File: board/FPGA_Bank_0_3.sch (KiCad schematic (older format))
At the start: 13 parts, among them U10 XC6SLX150T

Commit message: Issue #1458 - HDMI RX TX pins added, Cypress added, DDR added
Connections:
- net GTP1V2: now also U10.E9 (MGTRREF_101)
- net TX_LANEN2: now reaches U10.A14 (*MGTTXN0_123)
- net TX_LANEN3: now reaches U10.A16 (*MGTTXN1_123)
- net RXCONFIG1: now reaches U10.A18 (IO_L63N_SCP6_0)
- net TXHPD: now reaches U10.A19 (IO_L64N_SCP4_0)
- net TXAUXCH_N: now reaches U10.A20 (IO_L65N_SCP2_0)
- net TX_LANEN0: now reaches U10.A6 (MGTTXN0_101)
- net TX_LANEN1: now reaches U10.A8 (MGTTXN1_101)
- net TX_LANEP2: now reaches U10.B14 (*MGTTXP0_123)
- net TX_LANEP3: now reaches U10.B16 (*MGTTXP1_123)
- net RXCONFIG2: now reaches U10.B18 (IO_L63P_SCP7_0)
- net TXAUXCH_P: now reaches U10.B20 (IO_L65P_SCP3_0)
- net TX_LANEP0: now reaches U10.B6 (MGTTXP0_101)
- net TX_LANEP1: now reaches U10.B8 (MGTTXP1_101)
- net RX_LANEN2: now reaches U10.C13 (*MGTRXN0_123)
- net RX_LANEN3: now reaches U10.C15 (*MGTRXN1_123)
- net TXCONFIG1: now reaches U10.C18 (IO_L66N_SCP0_0)
- net RXHPD: now reaches U10.C19 (IO_L64P_SCP5_0)
- net RX_LANEN0: now reaches U10.C7 (MGTRXN0_101)
- net RX_LANEN1: now reaches U10.C9 (MGTRXN1_101)
- net RX_LANEP2: now reaches U10.D13 (*MGTRXP0_123)
- net RX_LANEP3: now reaches U10.D15 (*MGTRXP1_123)
- net TXCONFIG2: now reaches U10.D17 (IO_L66P_SCP1_0)
- net RXAUXCH_P: now reaches U10.D18 (IO_L62P_0)
- net RXAUXCH_N: now reaches U10.D19 (IO_L62N_VREF_0)
- net RX_LANEP0: now reaches U10.D7 (MGTRXP0_101)
- net RX_LANEP1: now reaches U10.D9 (MGTRXP1_101)
- net CLK1_N: no longer names the net of U10.B12 (*MGTREFCLK0N_123)
- net CLK1_P: no longer names the net of U10.A12 (*MGTREFCLK0P_123)
- net CLK2_N: no longer names the net of U10.F12 (*MGTREFCLK1N_123)
- net CLK2_P: no longer names the net of U10.E12 (*MGTREFCLK1P_123)
- net GPIO_N_48: no longer names the net of U10.P7 (*IO_L25N_3)
- net GPIO_N_49: no longer names the net of U10.T4 (*IO_L24N_3)
- net GPIO_N_50: no longer names the net of U10.N7 (*IO_L23N_3)
- net GPIO_N_51: no longer names the net of U10.AA1 (IO_L10N_3)
- net GPIO_N_52: no longer names the net of U10.P4 (IO_L9N_3)
- net GPIO_N_53: no longer names the net of U10.V3 (*IO_L8N_3)
- net GPIO_N_54: no longer names the net of U10.T5 (*IO_L7N_3)
- net GPIO_N_55: no longer names the net of U10.Y3 (IO_L2N_3)
- net GPIO_N_56: no longer names the net of U10.G4 (*IO_L58N_3)
- net GPIO_N_57: no longer names the net of U10.D1 (IO_L59N_3)
- net GPIO_N_58: no longer names the net of U10.E4 (IO_L60N_3)
- net GPIO_N_59: no longer names the net of U10.G7 (*IO_L80N_3)
- net GPIO_N_60: no longer names the net of U10.H8 (*IO_L81N_3)
- net GPIO_P_48: no longer names the net of U10.P6 (*IO_L25P_3)
- net GPIO_P_49: no longer names the net of U10.U4 (*IO_L24P_3)
- net GPIO_P_50: no longer names the net of U10.N6 (*IO_L23P_3)
- net GPIO_P_51: no longer names the net of U10.AA2 (IO_L10P_3)
- net GPIO_P_52: no longer names the net of U10.P5 (IO_L9P_3)
- net GPIO_P_53: no longer names the net of U10.V5 (*IO_L8P_3)
- net GPIO_P_54: no longer names the net of U10.T6 (*IO_L7P_3)
- net GPIO_P_55: no longer names the net of U10.W4 (IO_L2P_3)
- net GPIO_P_56: no longer names the net of U10.H4 (*IO_L58P_3)
- net GPIO_P_57: no longer names the net of U10.D2 (IO_L59P_3)
- net GPIO_P_58: no longer names the net of U10.F3 (IO_L60P_3)
- net GPIO_P_59: no longer names the net of U10.H6 (*IO_L80P_3)
- net GPIO_P_60: no longer names the net of U10.J7 (*IO_L81P_3)

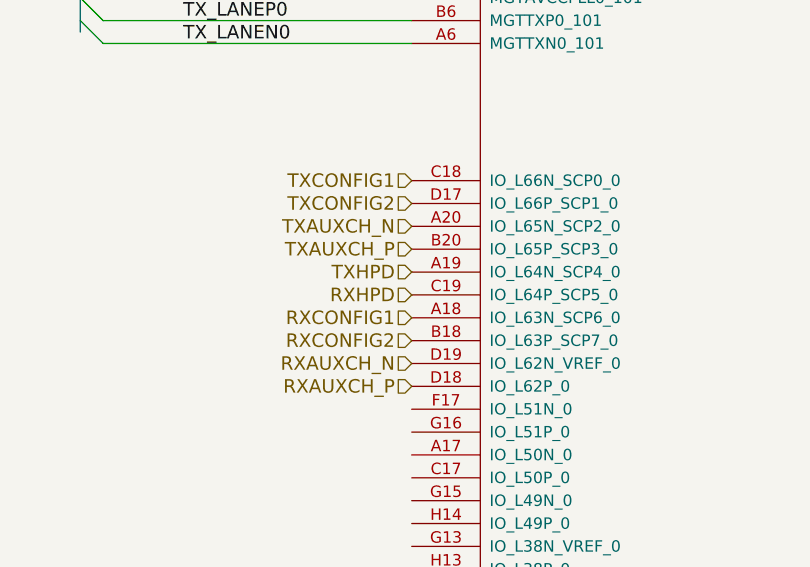
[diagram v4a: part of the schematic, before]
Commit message: Issue #1471 - usb Sheet changes
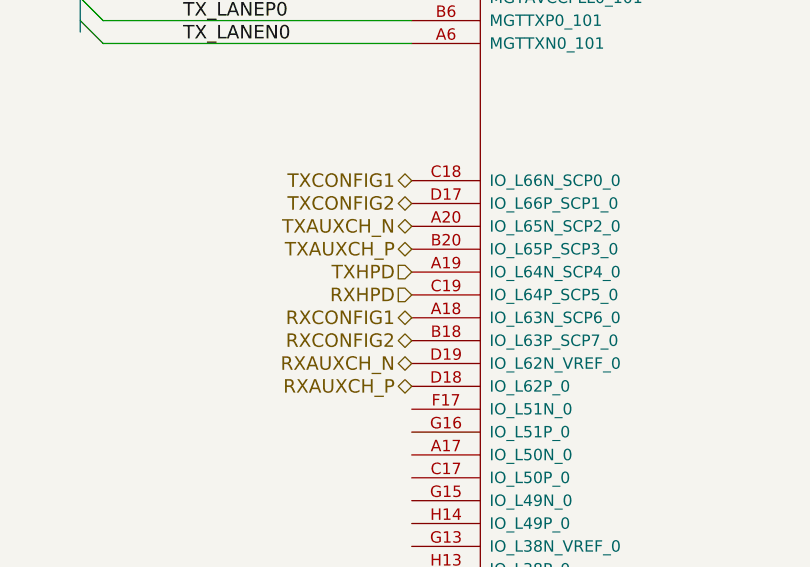
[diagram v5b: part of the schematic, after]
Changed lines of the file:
@@
 Text HLabel 17550 3800 0    59   BiDi ~ 0
 TX_LANEP[0..3]
-Text HLabel 19200 8450 0    59   Input ~ 0
+Text HLabel 19200 8450 0    59   BiDi ~ 0
 TXCONFIG1
-Text HLabel 19200 8550 0    59   Input ~ 0
+Text HLabel 19200 8550 0    59   BiDi ~ 0
 TXCONFIG2
-Text HLabel 19200 8750 0    59   Input ~ 0
+Text HLabel 19200 8750 0    59   BiDi ~ 0
 TXAUXCH_P
-Text HLabel 19200 8650 0    59   Input ~ 0
+Text HLabel 19200 8650 0    59   BiDi ~ 0
 TXAUXCH_N
 Text HLabel 19200 8850 0    59   Input ~ 0
 TXHPD
-Text HLabel 19200 9050 0    59   Input ~ 0
+Text HLabel 19200 9050 0    59   BiDi ~ 0
 RXCONFIG1
-Text HLabel 19200 9150 0    59   Input ~ 0
+Text HLabel 19200 9150 0    59   BiDi ~ 0
 RXCONFIG2
-Text HLabel 19200 9350 0    59   Input ~ 0
+Text HLabel 19200 9350 0    59   BiDi ~ 0
 RXAUXCH_P
-Text HLabel 19200 9250 0    59   Input ~ 0
+Text HLabel 19200 9250 0    59   BiDi ~ 0
 RXAUXCH_N
 Text HLabel 19200 8950 0    59   Input ~ 0

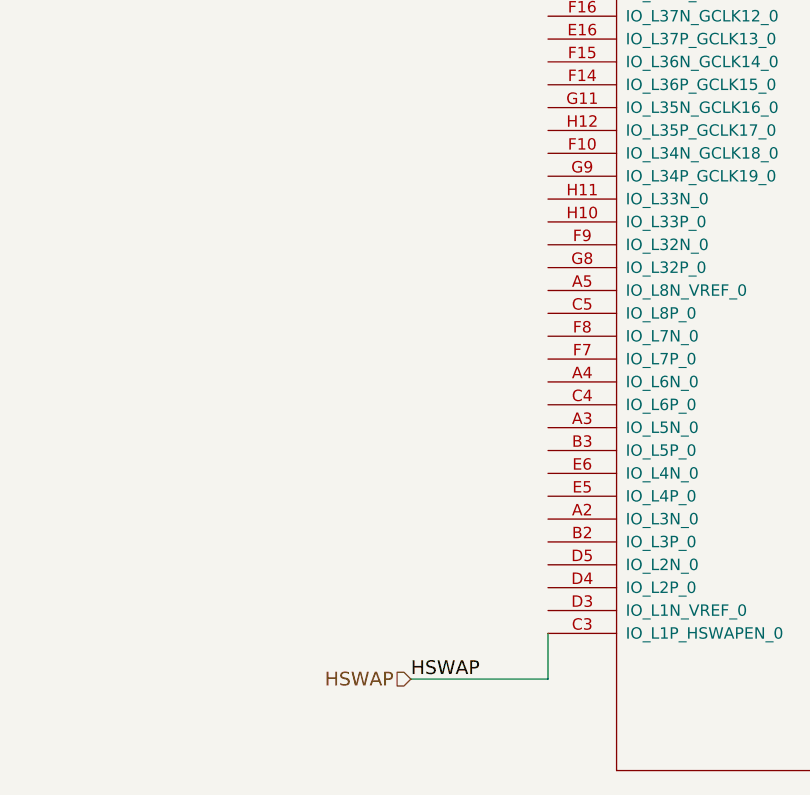
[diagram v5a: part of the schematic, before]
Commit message: Issue #1471 - USB schematic changes
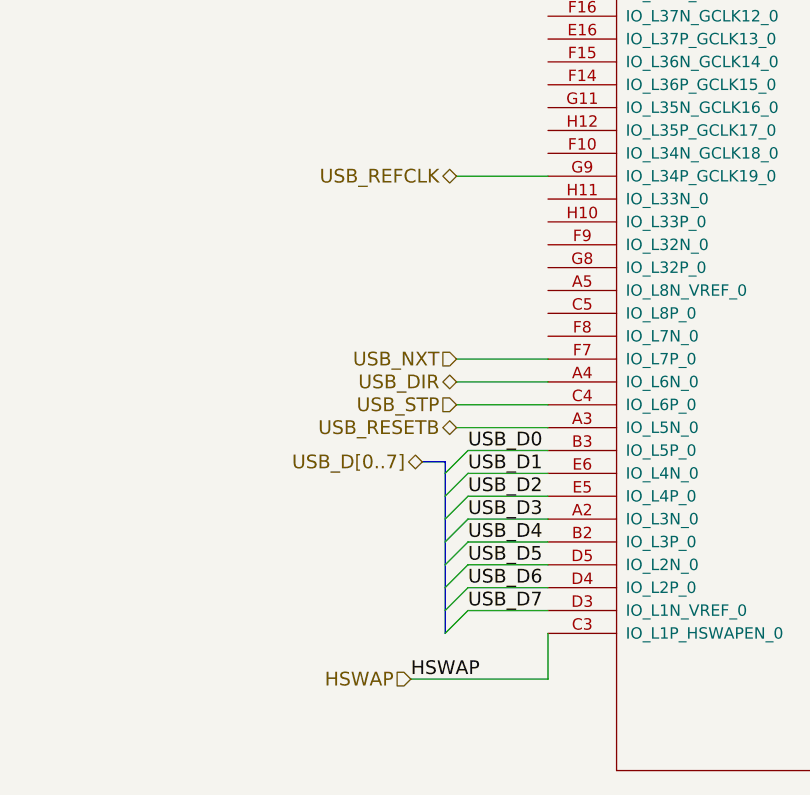
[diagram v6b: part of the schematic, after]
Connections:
- net USB_D3: now reaches U10.A2 (IO_L3N_0)
- net USB_RESETB: now reaches U10.A3 (IO_L5N_0)
- net USB_DIR: now reaches U10.A4 (IO_L6N_0)
- net USB_D4: now reaches U10.B2 (IO_L3P_0)
- net USB_D0: now reaches U10.B3 (IO_L5P_0)
- net USB_STP: now reaches U10.C4 (IO_L6P_0)
- net USB_D7: now reaches U10.D3 (IO_L1N_VREF_0)
- net USB_D6: now reaches U10.D4 (IO_L2P_0)
- net USB_D5: now reaches U10.D5 (IO_L2N_0)
- net USB_D2: now reaches U10.E5 (IO_L4P_0)
- net USB_D1: now reaches U10.E6 (IO_L4N_0)
- net USB_NXT: now reaches U10.F7 (IO_L7P_0)
- net USB_REFCLK: now reaches U10.G9 (IO_L34P_GCLK19_0)
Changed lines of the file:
@@
 Sheet 2 11
 Title "HDMI2USB"
-Date "30 dec 2014"
+Date "1 jan 2015"
 Rev "Rev2"
 Comp ""
@@
 Text HLabel 19200 8950 0    59   Input ~ 0
 RXHPD
+Text HLabel 18650 12200 0    60   BiDi ~ 0
+USB_D[0..7]
+Text Label 18850 12150 0    60   ~ 0
+USB_D0
+Text Label 18850 12250 0    60   ~ 0
+USB_D1
+Text Label 18850 12350 0    60   ~ 0
+USB_D2
+Text Label 18850 12450 0    60   ~ 0
+USB_D3
+Text Label 18850 12550 0    60   ~ 0
+USB_D4
+Text Label 18850 12650 0    60   ~ 0
+USB_D5
+Text Label 18850 12750 0    60   ~ 0
+USB_D6
+Text Label 18850 12850 0    60   ~ 0
+USB_D7
+Wire Wire Line
+	19200 12150 18850 12150
+Wire Wire Line
+	18850 12250 19200 12250
+Wire Wire Line
+	18850 12350 19200 12350
+Wire Wire Line
+	18850 12450 19200 12450
+Wire Wire Line
+	19200 12550 18850 12550
+Wire Wire Line
+	18850 12650 19200 12650
+Wire Wire Line
+	18850 12750 19200 12750
+Wire Wire Line
+	18850 12850 19200 12850
+Entry Wire Line
+	18750 12650 18850 12550
+Entry Wire Line
+	18750 12750 18850 12650
+Entry Wire Line
+	18750 12850 18850 12750
+Entry Wire Line
+	18750 12550 18850 12450
+Entry Wire Line
+	18750 12450 18850 12350
+Entry Wire Line
+	18750 12350 18850 12250
+Entry Wire Line
+	18750 12250 18850 12150
+Entry Wire Line
+	18750 12950 18850 12850
+Wire Bus Line
+	18750 12200 18750 12950
+Wire Bus Line
+	18750 12200 18650 12200
+Text HLabel 18800 11750 0    60   Input ~ 0
+USB_NXT
+Text HLabel 18800 11850 0    60   BiDi ~ 0
+USB_DIR
+Text HLabel 18800 11950 0    60   Input ~ 0
+USB_STP
+Text HLabel 18800 12050 0    60   BiDi ~ 0
+USB_RESETB
+Text HLabel 18800 10950 0    60   BiDi ~ 0
+USB_REFCLK
+Wire Wire Line
+	19200 10950 18800 10950
+Wire Wire Line
+	18800 12050 19200 12050
+Wire Wire Line
+	19200 11950 18800 11950
+Wire Wire Line
+	19200 11850 18800 11850
+Wire Wire Line
+	18800 11750 19200 11750
 $EndSCHEMATC
